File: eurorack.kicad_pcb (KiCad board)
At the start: 2 copper layers, 92 x 30 mm, 19 parts, among them J1 Eurorack 10-pin power, J2 to carrier row A (female 8.5m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, J3 to carrier row B (female 8.5m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, J4 to hat, above J2 (male), J5 to hat, above J3 (male), J6 IN 3.5mm mono, J7 OUT 3.5mm mono, J8 wires to hat J1/J2 pads, U1 K7805-1000R3

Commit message: display pass-through: J9 mates hat J6, J10 display socket, isolated DISP_* nets
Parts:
- J8: value wires to hat J1/J2 pads -> mates hat J7 (or wires to hat pads)
- moved D1 68.9 mm to (125.8, 66.8), turned to -90 degrees
- moved FB1 55.8 mm to (117.0, 68.8)
- moved R2 54.4 mm to (120.0, 43.0)
- moved R3 50.3 mm to (116.5, 42.8)
- moved C4 46.0 mm to (113.0, 42.8)
- moved R1 45.6 mm to (79.3, 68.5)
- moved C2 44.2 mm to (91.5, 67.8)
- moved J8 27.4 mm to (60.5, 64.8), turned to 90 degrees
- moved C3 23.9 mm to (85.0, 67.8)
- moved C1 18.3 mm to (72.5, 68.5)
- moved D2 11.4 mm to (61.4, 68.8)
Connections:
- J8 pad 3: AOUT_T -> AOUT_S
- J8 pad 4: AOUT_S -> AOUT_T

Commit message: layout: place and route the board; drop power LED and J9; display on main nets
- all nets routed, DRC clean (0 unconnected); audio in/out routed as tight
  signal+return pairs, input and output paths >=7mm apart
- single B.Cu GND pour over power + crossover; audio island pour-free,
  AIN_S/AOUT_S kept as separate returns end to end
- DISP_* nets merged into GND/+3V3/SCL/SDA: J10 powers and drives the
  display directly, hat J6 unneeded; J9 pass-through removed as redundant
- D2/R1 power LED dropped during layout; BOM synced
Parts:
- removed D2: green, LED_SMD:LED_0805_2012Metric
- removed R1: 2.2k, Resistor_SMD:R_0402_1005Metric
- added J10: display socket, Connector_PinSocket_2.54mm:PinSocket_1x04_P2.54mm_Vertical, F.Cu at (130.2, 59.8)
- D1: moved to B.Cu
- J6 (input): renamed from J6
- J7 (output): renamed from J7
- U1: moved to F.Cu
- moved R2 57.0 mm to (69.0, 68.5), turned to 180 degrees
- moved R3 53.4 mm to (69.0, 67.2)
- moved C1 34.1 mm to (104.8, 58.0), turned to -90 degrees
- moved C3 24.9 mm to (104.8, 52.8), turned to 90 degrees
- moved J4 24.7 mm to (116.3, 46.5), turned to -90 degrees
- moved J5 24.7 mm to (116.2, 64.4), turned to -90 degrees
- moved J3 23.4 mm to (148.1, 60.2), turned to 90 degrees
- moved J2 23.4 mm to (148.1, 42.5), turned to 90 degrees
- moved C2 17.7 mm to (106.2, 58.0), turned to -90 degrees
- moved FB1 16.8 mm to (100.2, 68.0), turned to 180 degrees
- moved J6 (input) 16.1 mm to (123.0, 64.0), turned to 0 degrees
- moved J7 (output) 15.7 mm to (123.0, 48.5), turned to 180 degrees
- moved U1 13.2 mm to (113.2, 58.0), turned to 90 degrees
- moved D1 12.3 mm to (113.5, 68.0), turned to 0 degrees
- moved C4 12.1 mm to (106.2, 52.8), turned to 90 degrees
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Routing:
- net +5V: track 0.00 -> 90.9 mm, vias 0 -> 2
- net AOUT_S: track 0.00 -> 76.2 mm
- net AOUT_T: track 0.00 -> 69.2 mm
- net LRCK: track 0.00 -> 68.8 mm, vias 0 -> 4
- net ASDOUT: track 0.00 -> 63.3 mm, vias 0 -> 1
- net AIN_JACK: track 0.00 -> 61.7 mm
- net AIN_S: track 0.00 -> 60.3 mm
- net PASS_B2: track 0.00 -> 53.9 mm
- net +3V3: track 0.00 -> 53.9 mm, vias 0 -> 3
- net DSDIN: track 0.00 -> 46.4 mm, vias 0 -> 2
- net PASS_B4: track 0.00 -> 43.1 mm
- net BCLK: track 0.00 -> 37.0 mm, vias 0 -> 2
- net SCL: track 0.00 -> 32.8 mm, vias 0 -> 2
- net MCLK: track 0.00 -> 32.7 mm, vias 0 -> 2
- net DET: track 0.00 -> 28.7 mm, vias 0 -> 2
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- added copper zone on B.Cu, net GND
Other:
- board size 92 x 30 mm -> 84.7 x 30 mm
- board text added: "5V (ETH board)"
- board text added: "5V (audio hat)"
- board text added: "Synthia v1"

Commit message: pcb: relocate buck to bottom side, extend GND pour over it; regen fab + docs
- U1 (K7805) moved to B.Cu on the west half with C1-C4/FB1 following,
  clearing the hat overhang; +5V rerouted, cap spacing fixed
- GND pour extended west over the buck cluster (return currents in
  copper, clear of both audio pairs); coupling audit re-passed, DRC clean
- regen gerbers/BOM/CPL, doc PDFs, board STEP; drop stale faceplate.svg
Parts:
- U1: moved to B.Cu
- moved U1 25.0 mm to (89.5, 66.0), turned to 0 degrees
- moved C2 22.6 mm to (85.2, 66.2), turned to 90 degrees
- moved C1 20.0 mm to (86.6, 66.2), turned to 90 degrees
- moved C3 15.5 mm to (97.3, 66.2), turned to -90 degrees
- moved C4 15.5 mm to (98.7, 66.2), turned to -90 degrees
- moved FB1 6.19 mm to (106.4, 68.0)
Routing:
- net +5V: track 90.9 -> 77.2 mm
- net LRCK: track 68.8 -> 56.7 mm, vias 4 -> 2
- net +12V_P: track 10.2 -> 4.02 mm
- net +12V_F: track 22.5 -> 21.8 mm

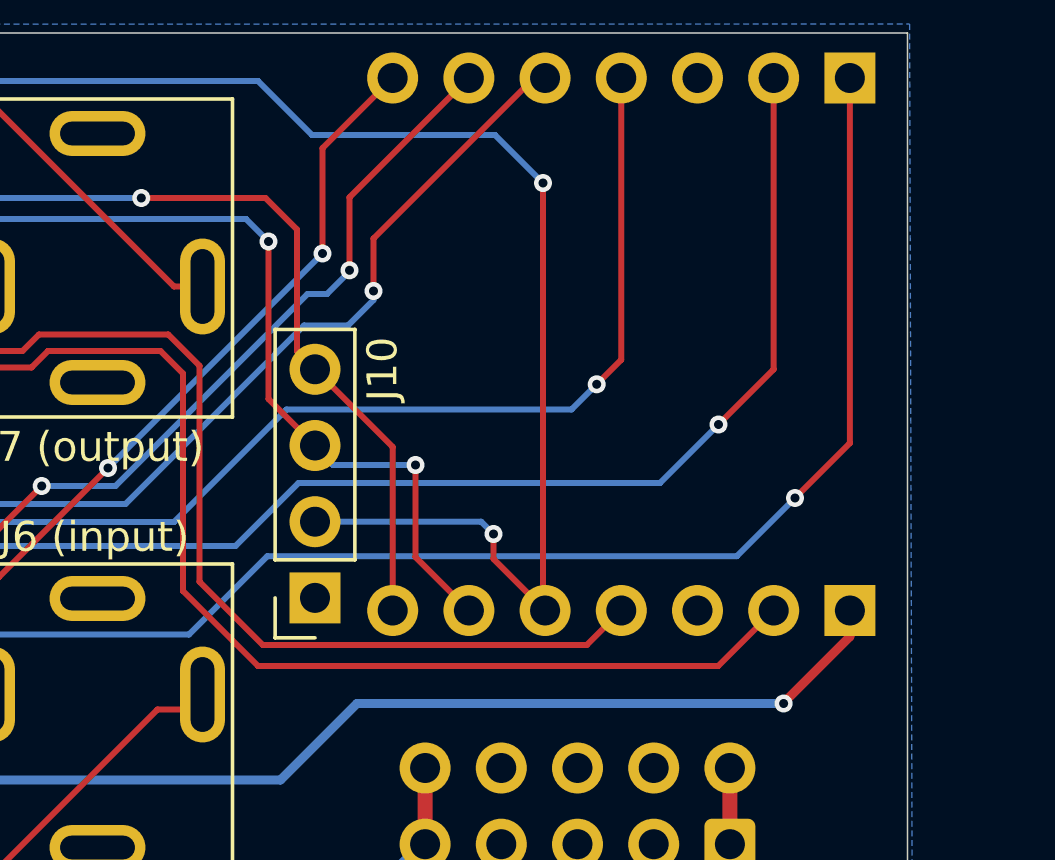
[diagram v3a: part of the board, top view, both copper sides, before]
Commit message: pcb: +3V3 reroute; regen fab + docs
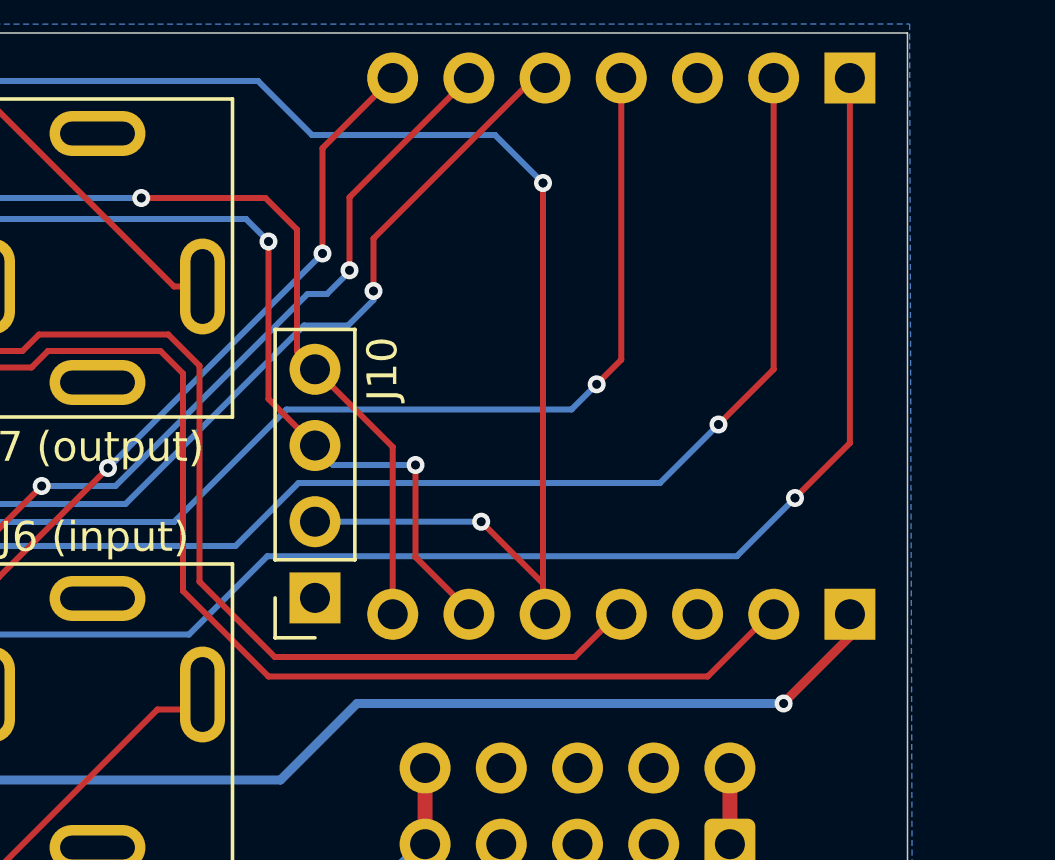
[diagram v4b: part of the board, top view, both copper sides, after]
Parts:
- moved J3 0.13 mm to (148.1, 60.4)
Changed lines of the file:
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@@
 	(footprint "Connector_PinSocket_2.54mm:PinSocket_1x07_P2.54mm_Vertical"
 		(layer "B.Cu")
-		(at 148.08 60.25 90)
+		(at 148.081454 60.375457 90)
 		(descr "Through hole straight socket strip, 1x07, 2.54mm pitch, single row (from Kicad 4.0.7), script generated")
 		(tags "Through hole socket strip THT 1x07 2.54mm single row")
@@
 	)
 	(segment
-		(start 137.85 46)
+		(start 137.85 59.35)
 		(end 137.85 60.18)
 		(width 0.2)
@@
 	)
 	(segment
-		(start 137.92 60.25)
-		(end 136.2 58.53)
+		(start 137.85 60.18)
+		(end 137.85 46)
 		(width 0.2)
 		(layer "F.Cu")
@@
 	)
 	(segment
-		(start 136.2 58.53)
-		(end 136.2 57.7)
-		(width 0.2)
-		(layer "F.Cu")
-		(net "+3V3")
-	)
-	(segment
 		(start 111.21 46.5)
 		(end 111.21 45.59)
@@
 	)
 	(segment
-		(start 137.85 60.18)
-		(end 137.92 60.25)
+		(start 135.79 57.29)
+		(end 137.85 59.35)
 		(width 0.2)
 		(layer "F.Cu")
@@
 	)
 	(via
-		(at 136.2 57.7)
+		(at 135.79 57.29)
 		(size 0.6)
 		(drill 0.3)
@@
 	)
 	(segment
-		(start 136.2 57.7)
-		(end 135.79 57.29)
+		(start 135.79 57.29)
+		(end 130.25 57.29)
 		(width 0.2)
 		(layer "B.Cu")
@@
 	)
 	(segment
-		(start 135.79 57.29)
-		(end 130.25 57.29)
-		(width 0.2)
-		(layer "B.Cu")
-		(net "+3V3")
-	)
-	(segment
 		(start 128.35 42.6)
 		(end 114.2 42.6)
@@
 	)
 	(segment
-		(start 115.2 48.7)
-		(end 110.87 48.7)
+		(start 138.91 61.8)
+		(end 128.91 61.8)
 		(width 0.2)
 		(layer "F.Cu")
@@
 	)
 	(segment
-		(start 126.4 52.092033)
-		(end 125.357967 51.05)
+		(start 115.2 48.7)
+		(end 110.87 48.7)
 		(width 0.2)
 		(layer "F.Cu")
@@
 	)
 	(segment
-		(start 120.5 51.6)
-		(end 118.1 51.6)
+		(start 121.05 51.05)
+		(end 120.5 51.6)
 		(width 0.2)
 		(layer "F.Cu")
@@
 	)
 	(segment
-		(start 128.51 61.4)
+		(start 128.91 61.8)
 		(end 126.4 59.29)
 		(width 0.2)
@@
 	)
 	(segment
-		(start 140.46 60.25)
-		(end 139.31 61.4)
+		(start 125.357967 51.05)
+		(end 121.05 51.05)
 		(width 0.2)
 		(layer "F.Cu")
@@
 	)
 	(segment
-		(start 126.4 59.29)
-		(end 126.4 52.092033)
+		(start 110.87 48.7)
+		(end 108.67 46.5)
 		(width 0.2)
 		(layer "F.Cu")
@@
 	)
 	(segment
-		(start 110.87 48.7)
-		(end 108.67 46.5)
+		(start 126.4 52.092033)
+		(end 125.357967 51.05)
 		(width 0.2)
 		(layer "F.Cu")
@@
 	)
 	(segment
-		(start 125.357967 51.05)
-		(end 121.05 51.05)
+		(start 140.46 60.25)
+		(end 138.91 61.8)
 		(width 0.2)
 		(layer "F.Cu")
@@
 	)
 	(segment
-		(start 118.1 51.6)
-		(end 115.2 48.7)
+		(start 120.5 51.6)
+		(end 118.1 51.6)
 		(width 0.2)
 		(layer "F.Cu")
@@
 	)
 	(segment
-		(start 139.31 61.4)
-		(end 128.51 61.4)
+		(start 126.4 59.29)
+		(end 126.4 52.092033)
 		(width 0.2)
 		(layer "F.Cu")
@@
 	)
 	(segment
-		(start 121.05 51.05)
-		(end 120.5 51.6)
+		(start 118.1 51.6)
+		(end 115.2 48.7)
 		(width 0.2)
 		(layer "F.Cu")
@@
 	)
 	(segment
-		(start 117.9 52.15)
-		(end 120.8 52.15)
+		(start 106.34 49.25)
+		(end 115 49.25)
 		(width 0.2)
 		(layer "F.Cu")
@@
 	)
 	(segment
-		(start 115 49.25)
-		(end 117.9 52.15)
+		(start 125.1 51.6)
+		(end 125.85 52.35)
 		(width 0.2)
 		(layer "F.Cu")
@@
 	)
 	(segment
-		(start 125.85 52.35)
-		(end 125.85 59.598529)
+		(start 121.35 51.6)
+		(end 125.1 51.6)
 		(width 0.2)
 		(layer "F.Cu")
@@
 	)
 	(segment
-		(start 120.8 52.15)
-		(end 121.35 51.6)
+		(start 125.85 52.35)
+		(end 125.85 59.598529)
 		(width 0.2)
 		(layer "F.Cu")
@@
 	)
 	(segment
-		(start 106.34 49.25)
-		(end 115 49.25)
+		(start 103.59 46.5)
+		(end 106.34 49.25)
 		(width 0.2)
 		(layer "F.Cu")
@@
 	)
 	(segment
-		(start 128.351471 62.1)
-		(end 143.69 62.1)
+		(start 143.34 62.45)
+		(end 145.54 60.25)
 		(width 0.2)
 		(layer "F.Cu")
@@
 	)
 	(segment
-		(start 103.59 46.5)
-		(end 106.34 49.25)
+		(start 125.85 59.598529)
+		(end 128.701471 62.45)
 		(width 0.2)
 		(layer "F.Cu")
@@
 	)
 	(segment
-		(start 143.69 62.1)
-		(end 145.54 60.25)
+		(start 128.701471 62.45)
+		(end 143.34 62.45)
 		(width 0.2)
 		(layer "F.Cu")
@@
 	)
 	(segment
-		(start 125.85 59.598529)
-		(end 128.351471 62.1)
+		(start 120.8 52.15)
+		(end 121.35 51.6)
 		(width 0.2)
 		(layer "F.Cu")
@@
 	)
 	(segment
-		(start 121.35 51.6)
-		(end 125.1 51.6)
+		(start 117.9 52.15)
+		(end 120.8 52.15)
 		(width 0.2)
 		(layer "F.Cu")
@@
 	)
 	(segment
-		(start 125.1 51.6)
-		(end 125.85 52.35)
+		(start 115 49.25)
+		(end 117.9 52.15)
 		(width 0.2)
 		(layer "F.Cu")
